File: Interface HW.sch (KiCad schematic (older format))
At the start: 8 parts

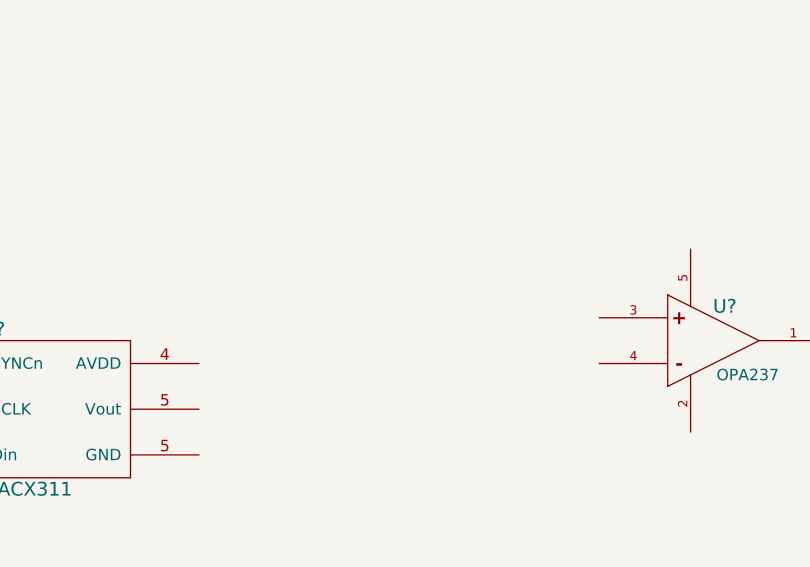
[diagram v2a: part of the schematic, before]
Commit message: Added resistor symbol
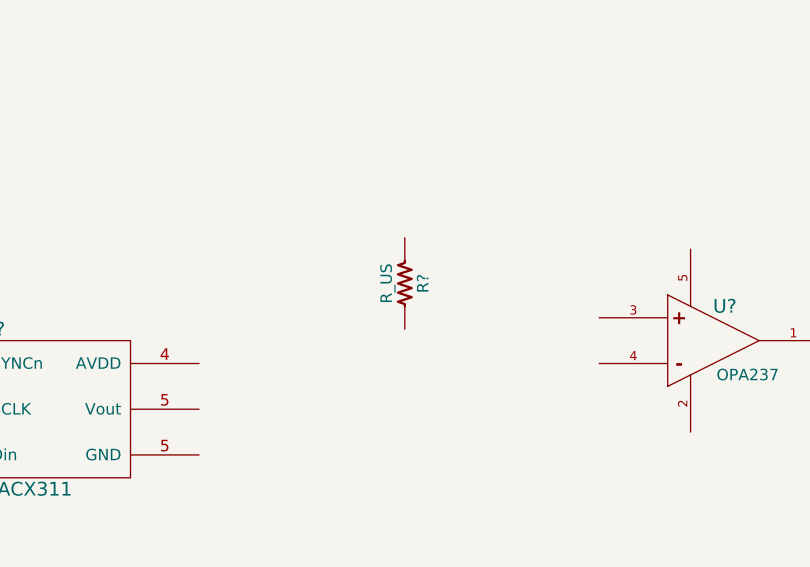
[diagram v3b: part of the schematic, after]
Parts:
- added R?: R_US, symbol R_US
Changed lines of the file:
@@
 LIBS:contrib
 LIBS:valves
+LIBS:diy_connectors
+LIBS:diy_diodes
+LIBS:diy_ics
+LIBS:diy_rcl
+LIBS:diy_regulators
+LIBS:diy_switches
+LIBS:diy_transformers
+LIBS:diy_transistors
+LIBS:diy_triac
+LIBS:diy_tubes
 LIBS:Interface HW-cache
 EELAYER 27 0
@@
 	1    0    0    -1
 $EndComp
+$Comp
+L R_US R?
+U 1 1 531E9055
+P 5750 3800
+F 0 "R?" V 5830 3800 50  0000 C CNN
+F 1 "R_US" V 5670 3800 50  0000 C CNN
+F 2 "" H 5750 3800 60  0000 C CNN
+F 3 "" H 5750 3800 60  0000 C CNN
+	1    5750 3800
+	1    0    0    -1
+$EndComp

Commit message: Added diff-amp circuit to schematic
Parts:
- removed U?: OPA237, symbol OPA237
- added C? (x3): 0.1uF, ~, symbol CSMALL
- added R? (x9): R_US, symbol R_US
- added TP?: TEST, symbol CONNECTOR
- added U? (x2): OPA237, symbol OPA237
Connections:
- wire segments 40 -> 98
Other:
- moved on the sheet: R?, U?

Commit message: Changed analog circuit to be differential output
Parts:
- removed R? (x4): R_US, symbol R_US
- removed U?: OPA237, symbol OPA237
- added R? (x12): R_US, symbol R_US
- added U? (x2): 74XXX1G32, symbol 74XXX1G32
- added U? (x3): OPA237, symbol OPA237
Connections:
- wire segments 98 -> 138
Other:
- note added: "SCL SDA USED AS GPIO"
- moved on the sheet: J?, R?, TP?, U?

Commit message: commit before attempting to add 2nd and 3rd page
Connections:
- net labels added: DAC_X
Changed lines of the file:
@@
 Sheet 1 1
 Title "Defcon Bot Interface Brd"
-Date "26 mar 2014"
+Date "27 mar 2014"
 Rev "1"
 Comp ""
@@
 	4550 6900 4850 6900
 Connection ~ 4550 6150
+Text GLabel 8200 2400 0    60   Input ~ 0
+DAC_X
 $EndSCHEMATC
